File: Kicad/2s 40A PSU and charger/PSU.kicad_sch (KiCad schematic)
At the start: 13 parts, among them U2 AP63203WU, U4 LP2981-3.3

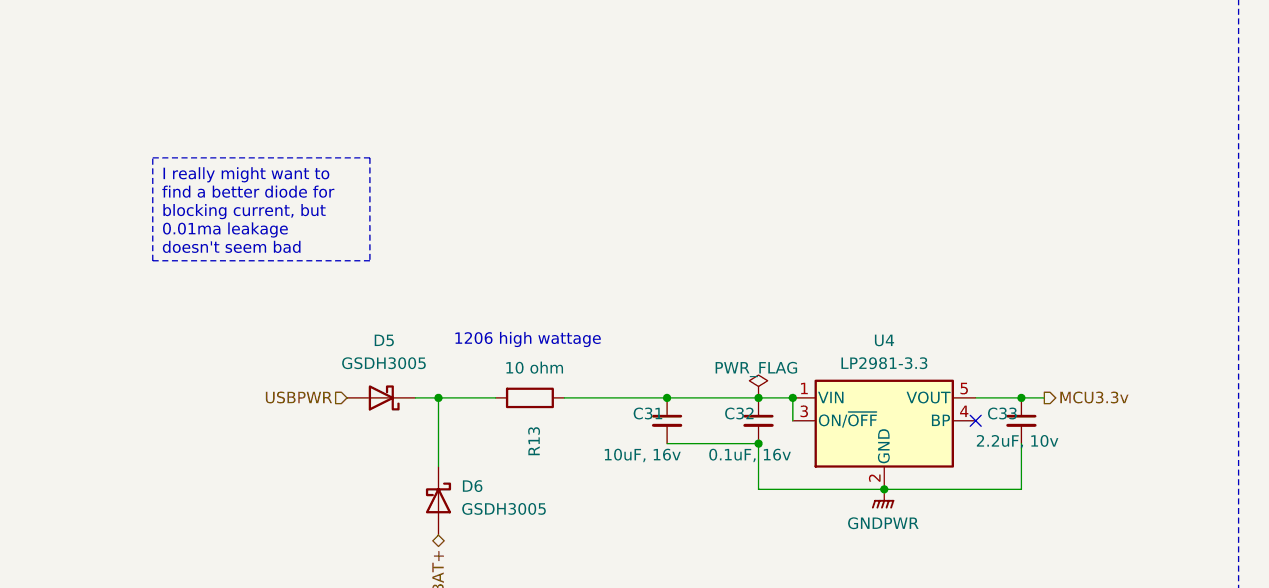
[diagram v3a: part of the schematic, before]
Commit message: Changed onboard mcu regulator
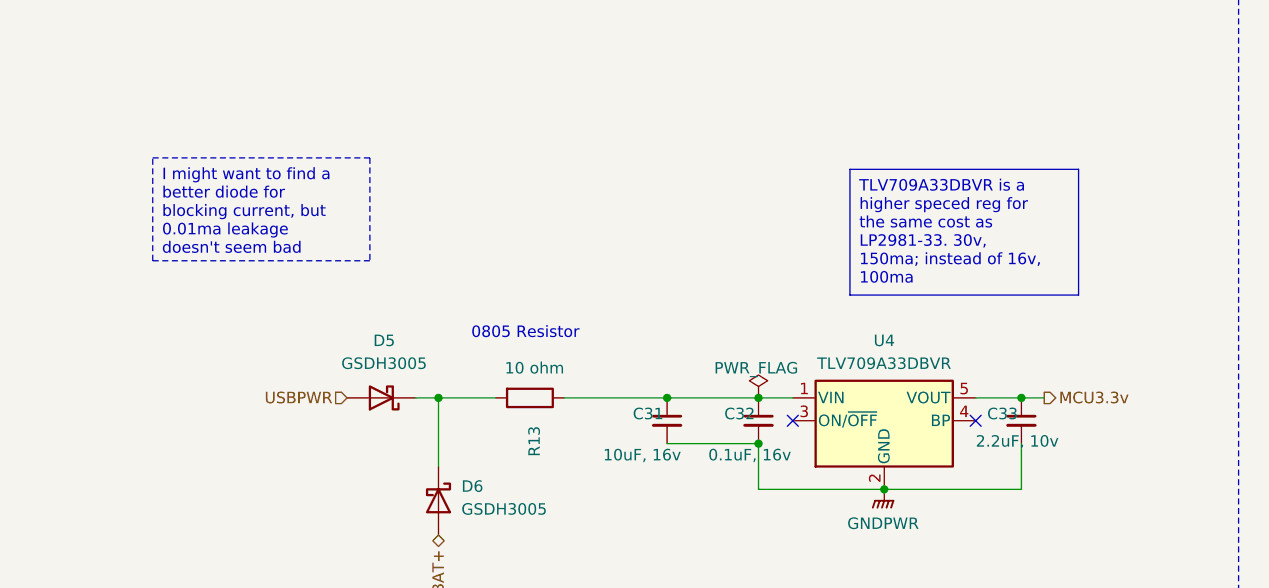
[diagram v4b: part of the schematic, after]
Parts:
- U4: value LP2981-3.3 -> TLV709A33DBVR
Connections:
- net at C31.1, C32.1, R13.1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: no longer U4.3 (ON/~{OFF})
- no-connect marks 1 -> 2
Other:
- note added: "0805 Resistor"
- note removed: "1206 high wattage"
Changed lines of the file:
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@@
 	(paper "A4")
 	(title_block
-		(date "2024-03-29")
+		(date "2024-11-28")
 		(rev "V1 Alpha")
 	)
@@
 	)
 	(junction
-		(at 97.79 74.93)
-		(diameter 0)
-		(color 0 0 0 0)
-	)
-	(junction
 		(at 243.84 76.2)
 		(diameter 0)
@@
 		(diameter 0)
 		(color 0 0 0 0)
+	)
+	(no_connect
+		(at 97.79 77.47)
 	)
 	(no_connect
@@
 	(wire
 		(pts
-			(xy 97.79 74.93) (xy 97.79 77.47)
-		)
-		(stroke
-			(width 0)
-			(type default)
-		)
-	)
-	(wire
-		(pts
 			(xy 179.07 86.36) (xy 195.58 86.36)
 		)
@@
 		)
 	)
-	(text_box "I really might want to find a better diode for blocking current, but 0.01ma leakage doesn't seem bad"
+	(text_box "TLV709A33DBVR is a higher speced reg for the same cost as LP2981-33. 30v, 150ma; instead of 16v, 100ma"
+		(exclude_from_sim no)
+		(at 104.14 49.53 0)
+		(size 25.4 13.97)
+		(stroke
+			(width 0)
+			(type default)
+		)
+		(fill
+			(type none)
+		)
+		(effects
+			(font
+				(size 1.27 1.27)
+			)
+			(justify left top)
+		)
+	)
+	(text_box "I might want to find a better diode for blocking current, but 0.01ma leakage doesn't seem bad"
 		(exclude_from_sim no)
 		(at 26.67 48.26 0)
@@
 		)
 	)
-	(text "1206 high wattage"
-		(exclude_from_sim no)
-		(at 68.326 68.58 0)
+	(text "0805 Resistor"
+		(exclude_from_sim no)
+		(at 68.072 67.818 0)
 		(effects
 			(font
@@
 			)
 		)
-		(property "Value" "LP2981-3.3"
+		(property "Value" "TLV709A33DBVR"
 			(at 107.95 71.12 0)
 			(effects
@@
 			)
 		)
-		(property "Datasheet" "http://www.ti.com/lit/ds/symlink/lp2981.pdf"
+		(property "Datasheet" "https://www.ti.com/lit/ds/symlink/tlv709.pdf"
 			(at 107.95 77.47 0)
 			(effects
@@
 			)
 		)
-		(property "Description" "150mA 16V Low-noise Low-dropout Regulator With Shutdown, 3.3V output voltage, SOT-23-5"
+		(property "Description" "150mA 30V Low-noise Low-dropout Regulator, 3.3V output voltage, SOT-23-5"
 			(at 107.95 77.47 0)
 			(effects

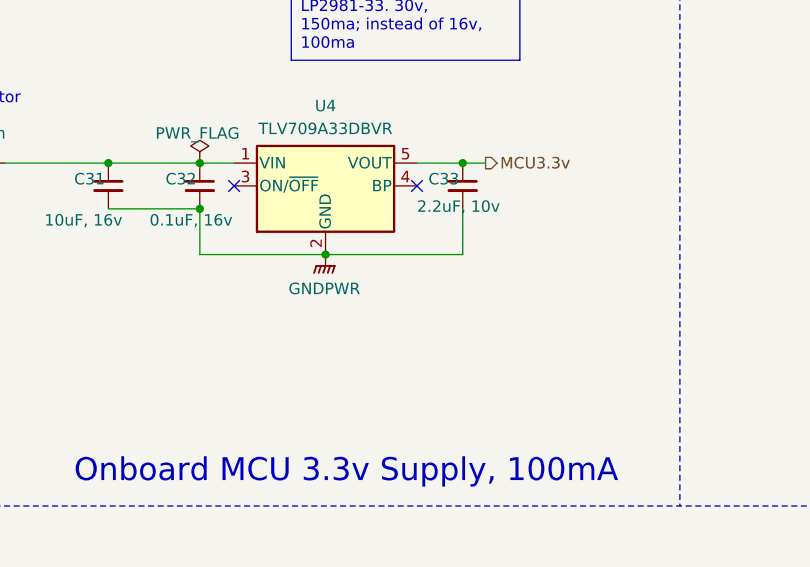
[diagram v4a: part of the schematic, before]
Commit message: Updated Ground connections and tweaked some formatting
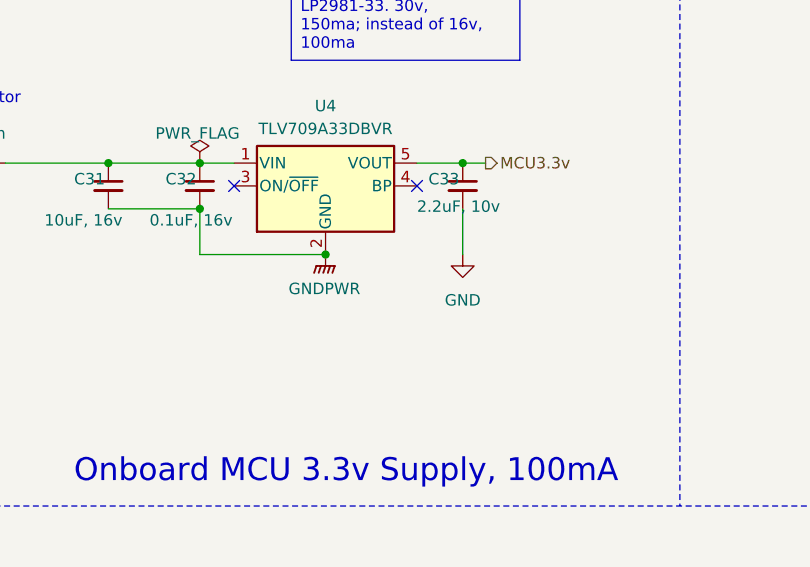
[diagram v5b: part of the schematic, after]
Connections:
- net GND: now also C33.2
- net GNDPWR: no longer C33.2
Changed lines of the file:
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@@
-	(wire
-		(pts
-			(xy 107.95 85.09) (xy 123.19 85.09)
-		)
-		(stroke
-			(width 0)
-			(type default)
-		)
-	)
 	(wire
 		(pts
@@
 					(unit 1)
 				)
+			)
+		)
+	)
+	(symbol
+		(lib_id "power:GND")
+		(at 123.19 85.09 0)
+		(unit 1)
+		(exclude_from_sim no)
+		(in_bom yes)
+		(on_board yes)
+		(dnp no)
+		(fields_autoplaced yes)
+		(property "Reference" "#PWR021"
+			(at 123.19 91.44 0)
+			(effects
+				(font
+					(size 1.27 1.27)
+				)
+				(hide yes)
+			)
+		)
+		(property "Value" "GND"
+			(at 123.19 90.17 0)
+			(effects
+				(font
+					(size 1.27 1.27)
+				)
+			)
+		)
+		(property "Footprint" ""
+			(at 123.19 85.09 0)
+			(effects
+				(font
+					(size 1.27 1.27)
+				)
+				(hide yes)
+			)
+		)
+		(property "Datasheet" ""
+			(at 123.19 85.09 0)
+			(effects
+				(font
+					(size 1.27 1.27)
+				)
+				(hide yes)
+			)
+		)
+		(property "Description" "Power symbol creates a global label with name \"GND\" , ground"
+			(at 123.19 85.09 0)
+			(effects
+				(font
+					(size 1.27 1.27)
+				)
+				(hide yes)
+			)
+		)
+		(pin "1"
+		)
+		(instances
+			(project "2s 40A PSU and charger"
+				(path "/eb3f183d-8bb1-43a5-a363-092ed67891e3/a57a0b4f-e246-497c-8d94-688647d8fd03"
+					(reference "#PWR021")
+					(unit 1)
+				)

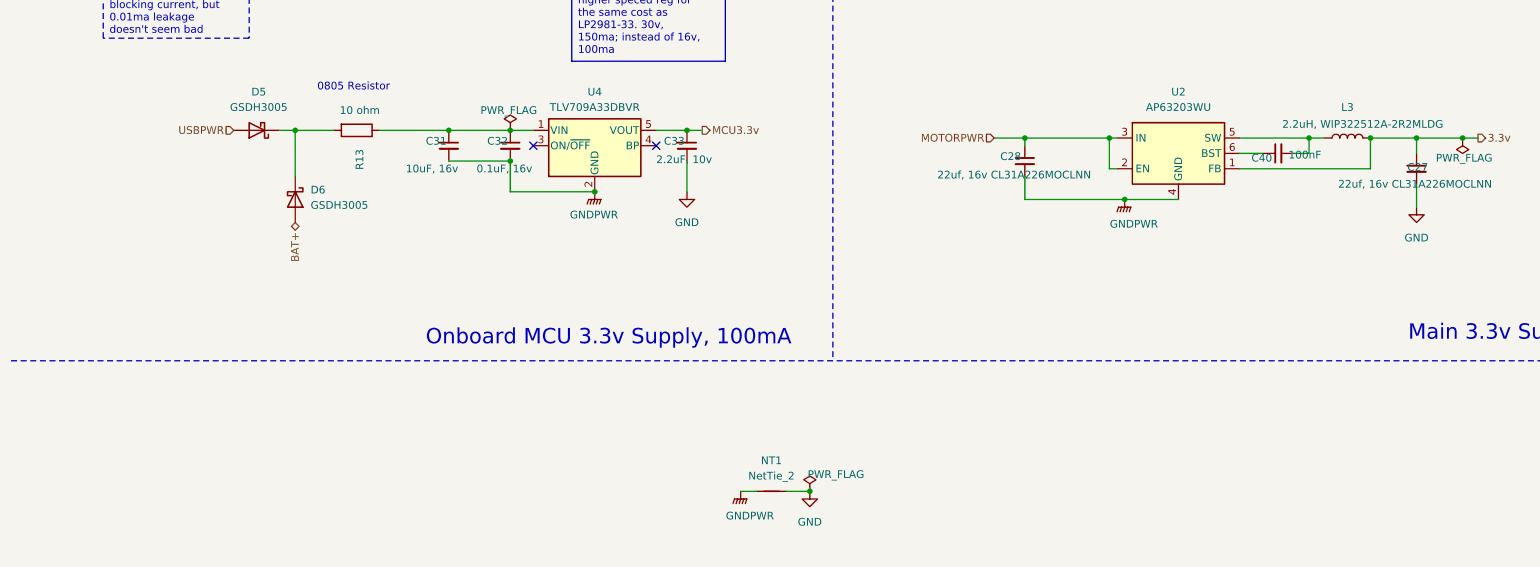
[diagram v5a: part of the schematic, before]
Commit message: Added use of Net Class Directives to speed up routing
I don't have to manually change wire sizes now
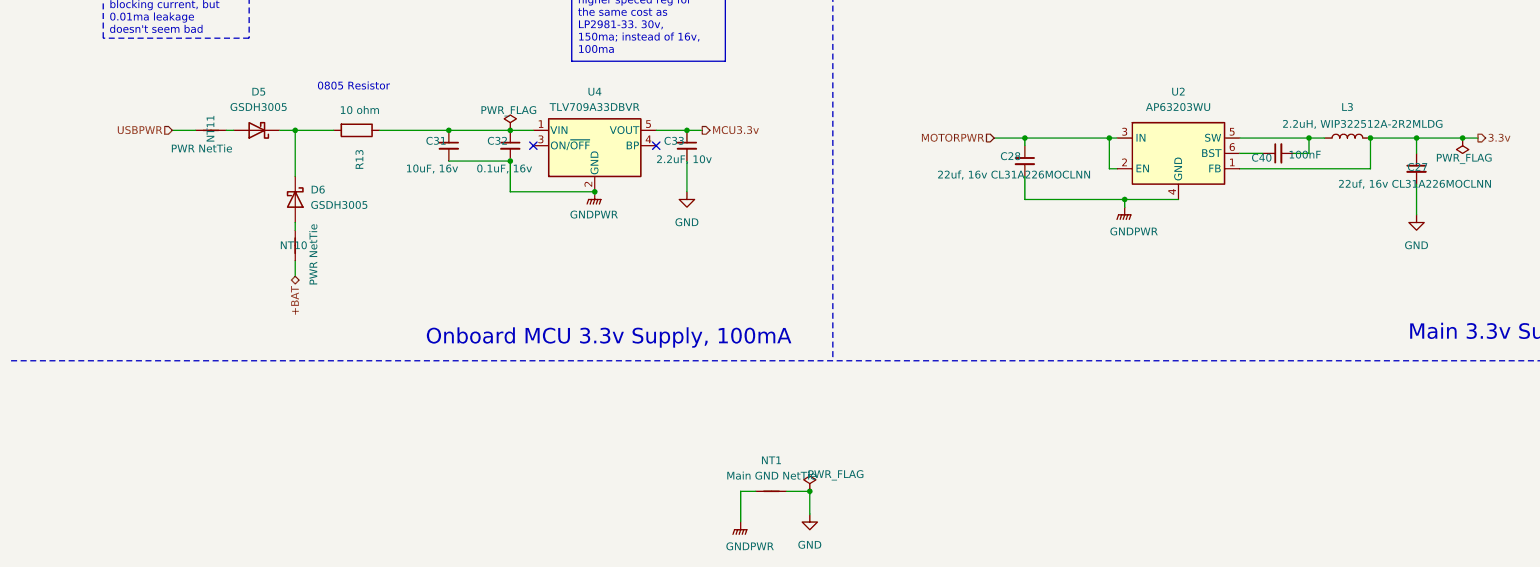
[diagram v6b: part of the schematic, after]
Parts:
- added NT10, NT11: PWR NetTie, custom_Connector:NetTie-2_SMD_Pad0.28mm, symbol Device:NetTie_2
- NT1: value NetTie_2 -> Main GND NetTie; footprint NetTie:NetTie-2_SMD_Pad0.5mm -> NetTie:NetTie-2_SMD_Pad2.0mm
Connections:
- net USBPWR: now also NT11.2; no longer D5.2 (A)
- net BAT+: no longer names the net of D6.2 (A)
- net BAT+: now also NT10.1
- new net: D5.2 (A), NT11.1
- new net +BAT: NT10.2

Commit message: Updated Sheet Properties
My author name is now in there, and I've added the proper project name.
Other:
- title: (none) -> CACKLE 2s 40A PSU & Charger
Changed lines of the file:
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@@
 	(paper "A4")
 	(title_block
-		(date "2024-11-28")
-		(rev "V1 Alpha")
+		(title "CACKLE 2s 40A PSU & Charger")
+		(date "2024-12-01")
+		(rev "V1")
+		(comment 1 "Author: Asher Edwards")
 	)
 	(junction

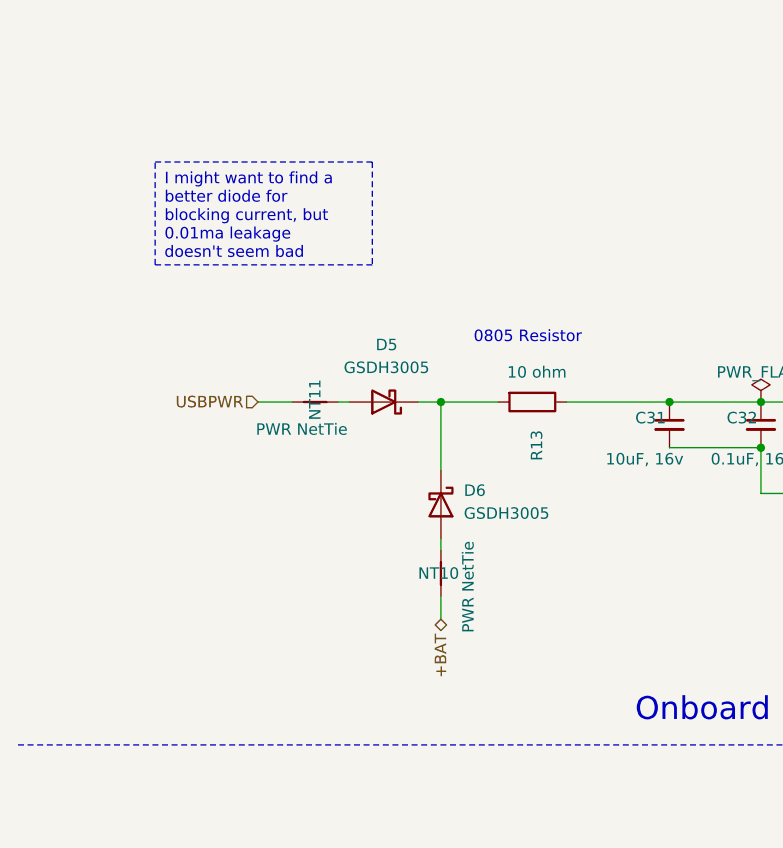
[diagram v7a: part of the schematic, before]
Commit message: Merged Always on PWR for multiple devices
The diode OR and the 10 ohm resistor are now shared between the MCU and the battery charger
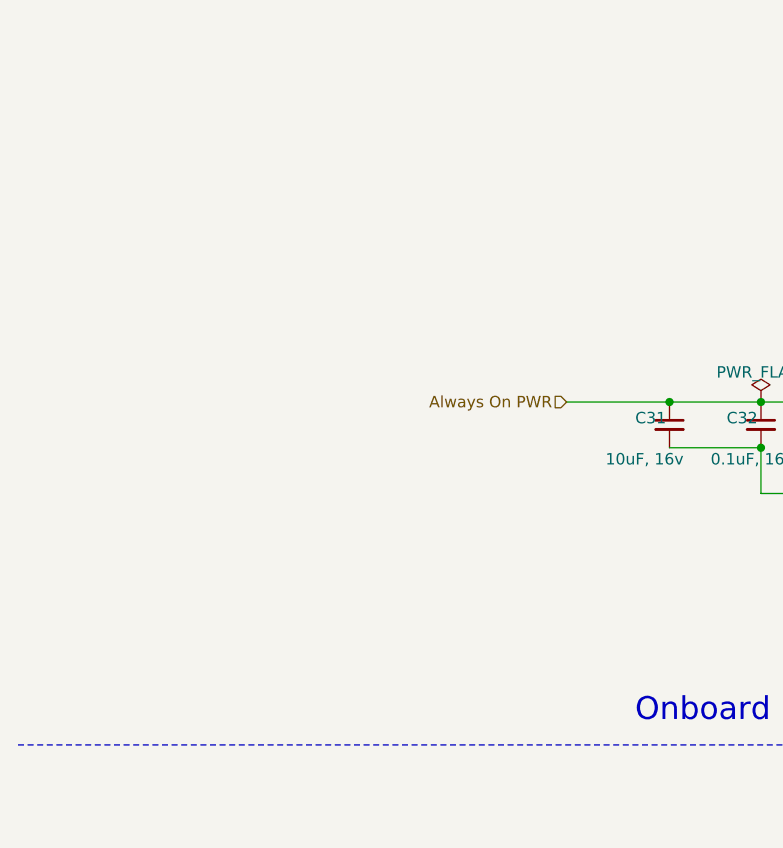
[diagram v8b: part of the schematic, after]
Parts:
- removed D5, D6: GSDH3005, Diode_SMD:D_0402_1005Metric, symbol Device:D_Schottky
- removed NT10, NT11: PWR NetTie, custom_Connector:NetTie-2_SMD_Pad0.28mm, symbol Device:NetTie_2
- removed R13: 10 ohm, Resistor_SMD:R_0805_2012Metric, symbol Device:R
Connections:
- net Always On PWR: now reaches C31.1, C32.1, U4.1 (VIN)
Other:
- note removed: "0805 Resistor"
